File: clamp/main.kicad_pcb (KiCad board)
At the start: 2 copper layers, 36 parts, among them P1 CONN_01X12, U1 LM741, U2 LM741, U3 LM741, U4 LM741, U5 LM741, U6 LM741

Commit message: update
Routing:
- net -VE: track 307.7 -> 304.4 mm
- net OUT: track 192.5 -> 189.2 mm
- net +VE: track 291.6 -> 288.6 mm
- net I-SET: track 34.3 -> 33.3 mm
- net V-SET: track 48.0 -> 48.9 mm

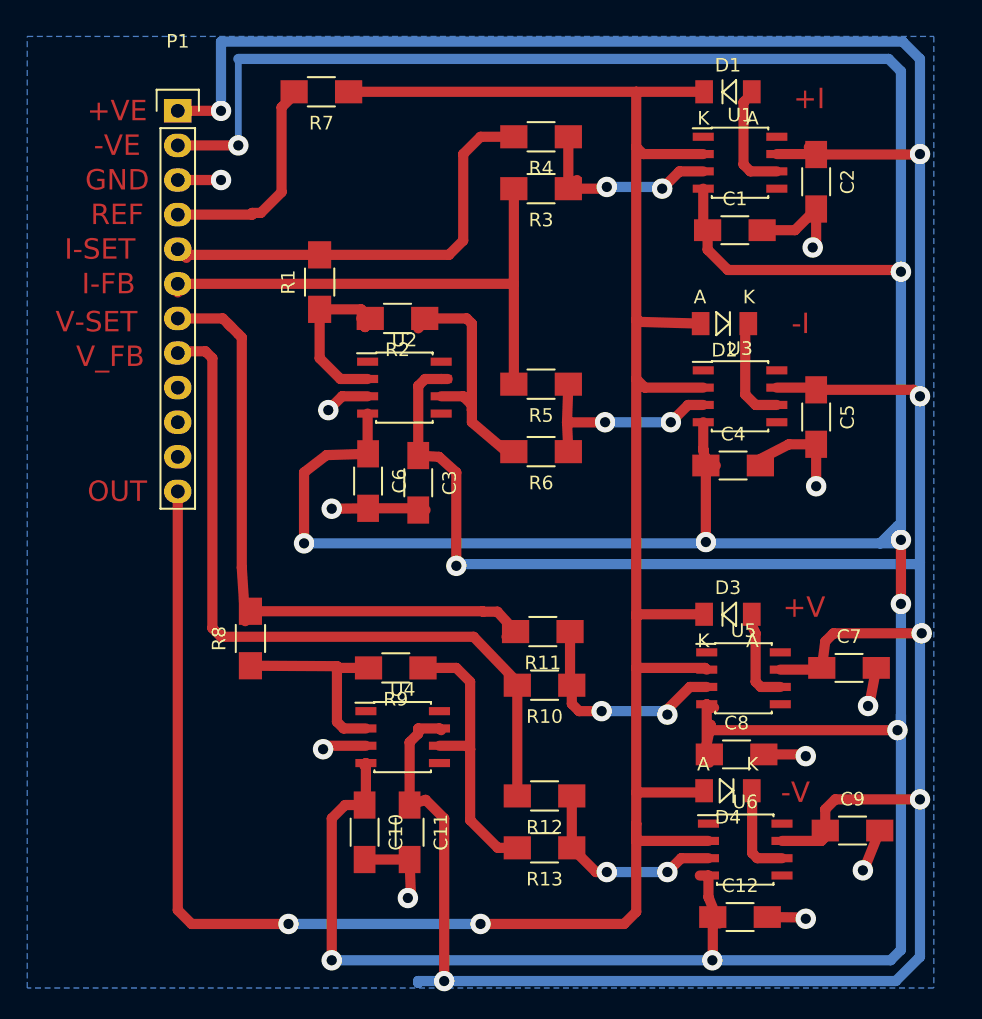
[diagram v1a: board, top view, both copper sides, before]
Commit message: add 0R values
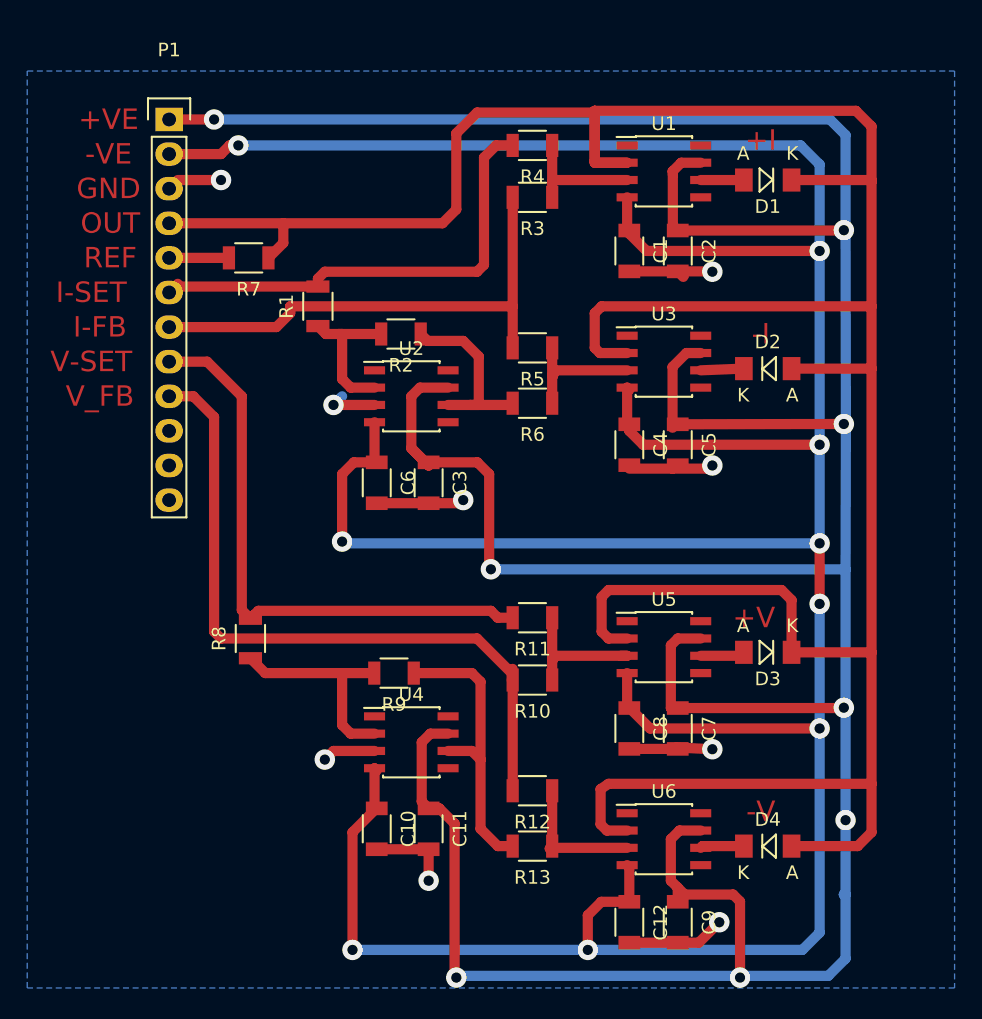
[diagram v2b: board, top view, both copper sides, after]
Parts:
- C1, C10, C11, C12, C2, C3, C4, C5, C6, C7, C8, C9: footprint Capacitors_SMD:C_1206_HandSoldering -> Capacitors_SMD:C_1206
- R1, R10, R11, R12, R13, R2, R3, R4, R5, R6, R7, R8, R9: footprint Resistors_SMD:R_1206_HandSoldering -> Resistors_SMD:R_1206
- moved C9 14.5 mm to (155.4, 145.3), turned to 270 degrees
- moved C7 13.3 mm to (155.4, 131.1), turned to 270 degrees
- moved R7 13.3 mm to (124.0, 96.5)
- moved C2 11.4 mm to (155.4, 96.0)
- moved C5 10.4 mm to (155.4, 110.2)
- moved C12 8.14 mm to (151.9, 145.3), turned to 270 degrees
- moved C8 8.10 mm to (151.9, 131.1), turned to 270 degrees
- moved C1 7.90 mm to (151.9, 96.0), turned to 270 degrees
- moved C4 7.77 mm to (151.9, 110.2), turned to 270 degrees
- moved D1 7.11 mm to (162.1, 90.8), turned to 180 degrees
- moved U5 6.27 mm to (154.4, 125.1)
- moved U3 6.14 mm to (154.4, 104.1)
- moved U6 6.02 mm to (154.4, 139.2)
- moved U1 5.62 mm to (154.4, 90.2)
- moved D4 5.00 mm to (162.1, 139.7), turned to 0 degrees
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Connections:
- P1 pad 12: OUT -> (no net)
- P1 pad 4: REF -> OUT
- P1 pad 5: I-SET -> REF
- P1 pad 6: I-FB -> I-SET
- P1 pad 7: V-SET -> I-FB
- P1 pad 8: V-FB -> V-SET
- P1 pad 9: (no net) -> V-FB
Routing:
- net -VE: track 304.4 -> 263.5 mm
- net OUT: track 189.2 -> 223.4 mm, vias 2 -> 0
- net REF: track 16.3 -> 4.72 mm
- net Net-(R10-Pad1): track 17.7 -> 10.8 mm, vias 2 -> 0
- net Net-(R3-Pad1): track 15.2 -> 9.36 mm, vias 2 -> 0
- net V-SET: track 48.9 -> 43.3 mm
- net V-FB: track 58.0 -> 52.3 mm
- net Net-(R5-Pad1): track 15.5 -> 9.90 mm, vias 2 -> 0
- net Net-(R12-Pad1): track 15.6 -> 10.1 mm, vias 2 -> 0
- net Net-(D1-Pad2): track 8.46 -> 3.17 mm
- net Net-(D2-Pad1): track 7.94 -> 3.17 mm
- net Net-(R2-Pad1): track 18.1 -> 13.9 mm
- net Net-(D4-Pad1): track 6.93 -> 3.22 mm
- net Net-(D3-Pad2): track 6.98 -> 3.28 mm
- net I-FB: track 40.4 -> 37.2 mm
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
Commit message: increased vias
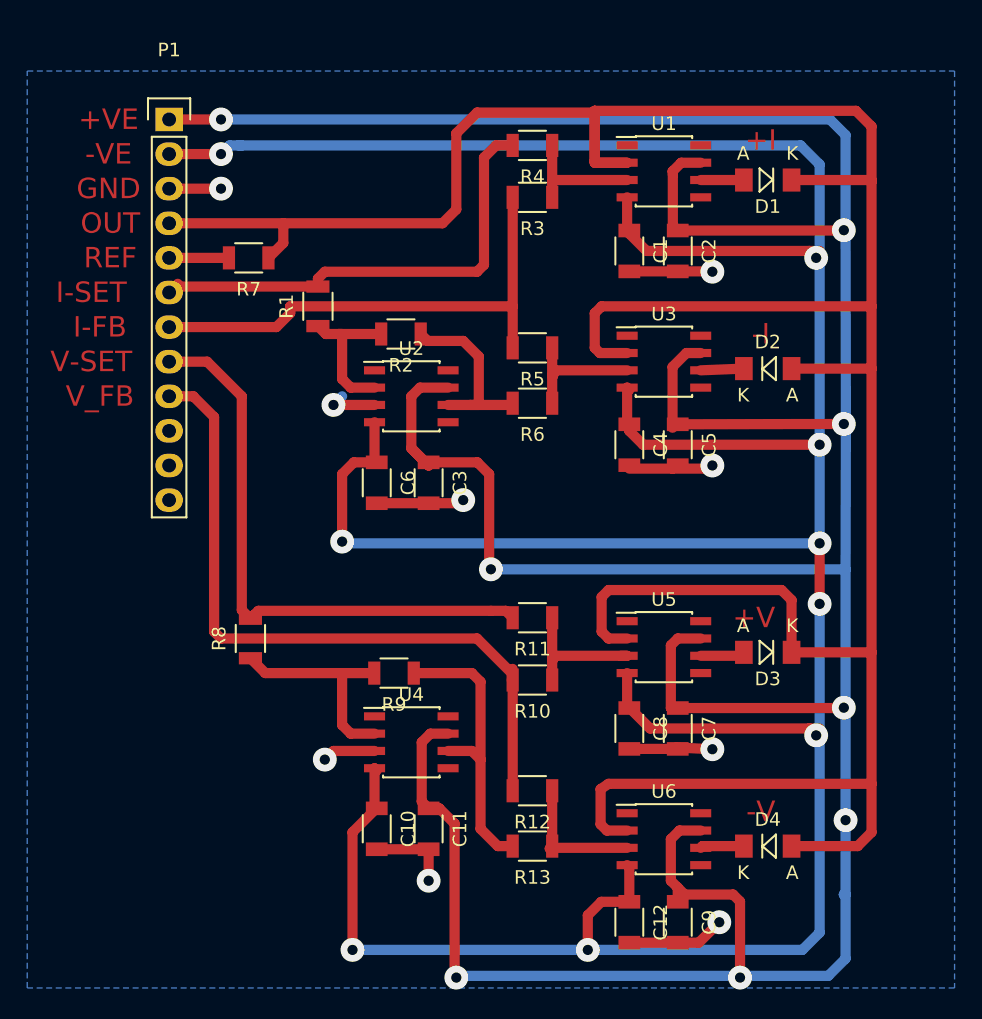
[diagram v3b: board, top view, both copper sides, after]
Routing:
- net -VE: track 263.5 -> 266.7 mm
- net GND: track 50.1 -> 49.4 mm
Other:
- net class Default: via_dia 1.5 -> 1.75

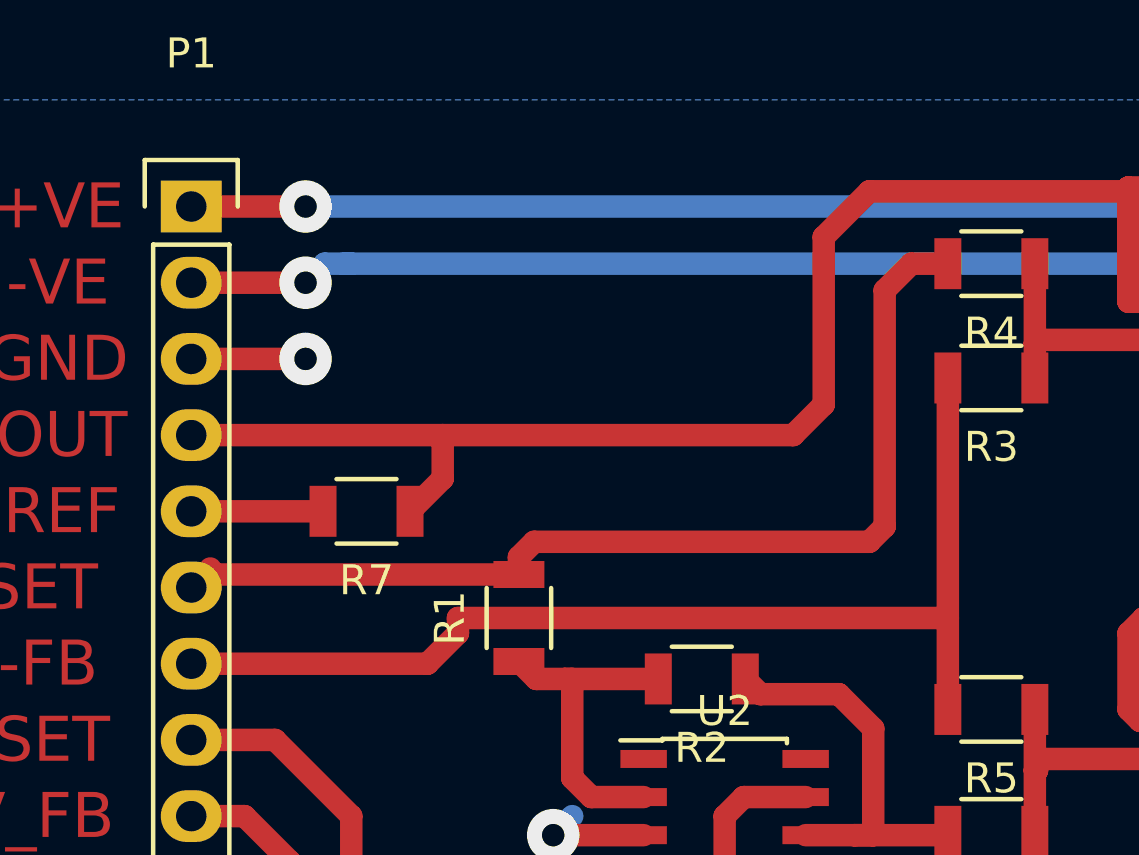
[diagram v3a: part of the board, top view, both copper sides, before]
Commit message: added heirarchical sheet
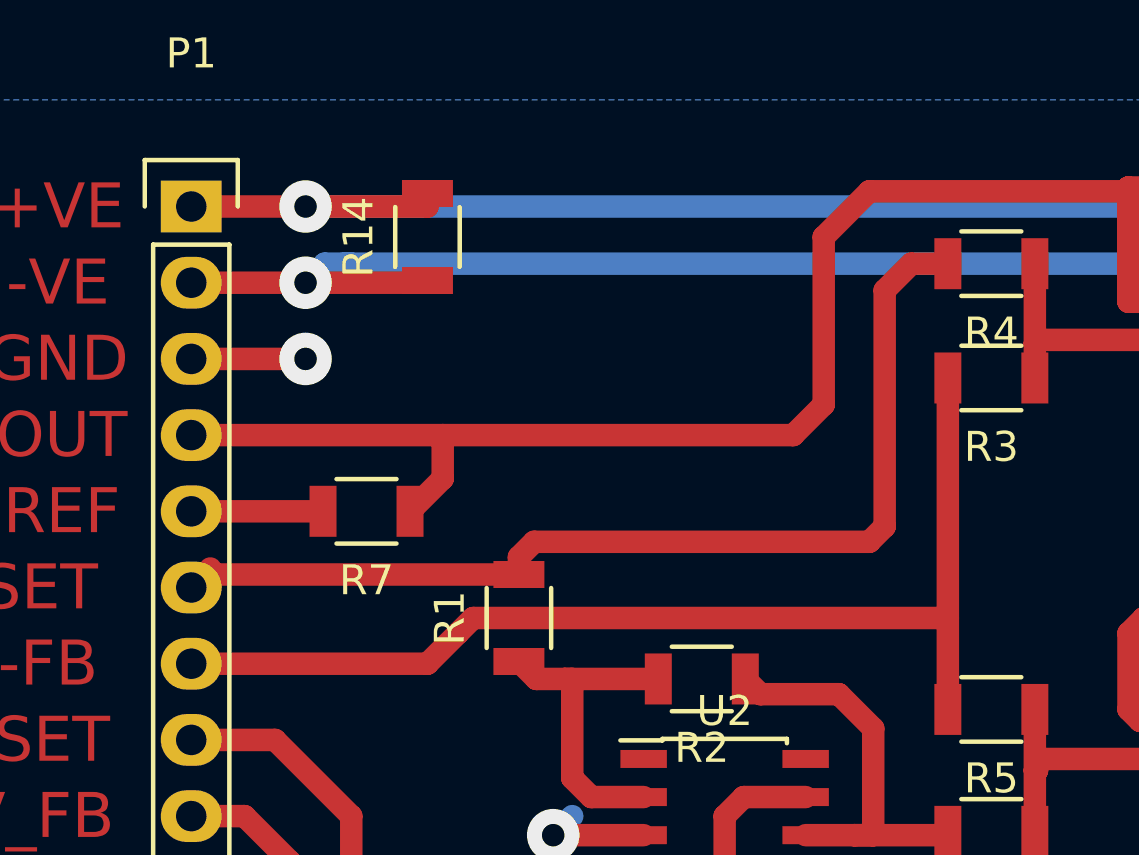
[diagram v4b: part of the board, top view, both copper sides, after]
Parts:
- added R14: R, Resistors_SMD:R_1206, F.Cu at (126.0, 87.4)
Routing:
- net +VE: track 287.6 -> 292.1 mm
- net -VE: track 266.7 -> 270.8 mm
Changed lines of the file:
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@@
 (kicad_pcb (version 4) (host pcbnew 4.0.4+dfsg1-stable)
   (general
-    (links 76)
+    (links 78)
     (no_connects 0)
-    (area 107.696 79.985 175.768001 151.352002)
+    (area 107.696 71.442999 175.768001 151.352002)
     (thickness 1.6)
     (drawings 13)
-    (tracks 339)
+    (tracks 343)
     (zones 0)
-    (modules 36)
+    (modules 37)
     (nets 22)
   )
@@
   (layers
     (0 F.Cu signal)
-    (31 B.Cu signal)
+    (31 B.Cu signal hide)
     (32 B.Adhes user)
     (33 F.Adhes user)
@@
     )
   )
+  (module Resistors_SMD:R_1206 (layer F.Cu)
+    (at 125.984 87.376 90)
+    (descr "Resistor SMD 1206, reflow soldering, Vishay (see dcrcw.pdf)")
+    (tags "resistor 1206")
+    (attr smd)
+    (fp_text reference R14 (at 0 -2.3 90) (layer F.SilkS)
+      (effects (font (size 1 1) (thickness 0.15)))
+    )
+    (fp_text value R (at 0 2.3 90) (layer F.Fab)
+      (effects (font (size 1 1) (thickness 0.15)))
+    )
+    (fp_line (start -2.2 -1.2) (end 2.2 -1.2) (layer F.CrtYd) (width 0.05))
+    (fp_line (start -2.2 1.2) (end 2.2 1.2) (layer F.CrtYd) (width 0.05))
+    (fp_line (start -2.2 -1.2) (end -2.2 1.2) (layer F.CrtYd) (width 0.05))
+    (fp_line (start 2.2 -1.2) (end 2.2 1.2) (layer F.CrtYd) (width 0.05))
+    (fp_line (start 1 1.075) (end -1 1.075) (layer F.SilkS) (width 0.15))
+    (fp_line (start -1 -1.075) (end 1 -1.075) (layer F.SilkS) (width 0.15))
+    (pad 1 smd rect (at -1.45 0 90) (size 0.9 1.7) (layers F.Cu F.Paste F.Mask)
+      (net 2 -VE))
+    (pad 2 smd rect (at 1.45 0 90) (size 0.9 1.7) (layers F.Cu F.Paste F.Mask)
+      (net 1 +VE))
+    (model Resistors_SMD.3dshapes/R_1206.wrl
+      (at (xyz 0 0 0))
+      (scale (xyz 1 1 1))
+      (rotate (xyz 0 0 0))
+    )
+  )
   (gr_text -V (at 161.544 137.16) (layer F.Cu)
     (effects (font (size 1.5 1.5) (thickness 0.3)))
@@
     (effects (font (size 1.5 1.5) (thickness 0.3)))
   )
+  (segment (start 121.92 86.36) (end 125.984 86.36) (width 0.75) (layer F.Cu) (net 1))
+  (segment (start 125.984 86.36) (end 125.984 85.926) (width 0.75) (layer F.Cu) (net 1))
   (segment (start 155.448 142.748) (end 155.448 143.788) (width 0.75) (layer F.Cu) (net 1))
   (segment (start 154.94 142.24) (end 155.448 142.748) (width 0.75) (layer F.Cu) (net 1))
@@
   (segment (start 135.89 106.68) (end 135.89 110.49) (width 0.75) (layer F.Cu) (net 1))
   (segment (start 136.525 106.045) (end 135.89 106.68) (width 0.75) (layer F.Cu) (net 1))
+  (segment (start 121.92 88.9) (end 125.91 88.9) (width 0.75) (layer F.Cu) (net 2))
+  (segment (start 125.91 88.9) (end 125.984 88.826) (width 0.75) (layer F.Cu) (net 2))
   (segment (start 165.1 131.064) (end 165.608 131.572) (width 0.75) (layer F.Cu) (net 2))
   (via (at 165.608 131.572) (size 1.75) (drill 0.75) (layers F.Cu B.Cu) (net 2))
@@
   (segment (start 118.544 98.626) (end 118.11 99.06) (width 0.75) (layer F.Cu) (net 8) (status 30))
   (segment (start 118.745 99.06) (end 118.745 98.425) (width 0.75) (layer F.Cu) (net 8) (status 30))
-  (segment (start 118.11 101.6) (end 125.984 101.6) (width 0.75) (layer F.Cu) (net 9) (status 10))
-  (segment (start 127 100.584) (end 127 100.076) (width 0.75) (layer F.Cu) (net 9))
+  (segment (start 127.508 100.076) (end 127 100.584) (width 0.75) (layer F.Cu) (net 9))
   (segment (start 125.984 101.6) (end 127 100.584) (width 0.75) (layer F.Cu) (net 9))
-  (segment (start 143.33 100.076) (end 127 100.076) (width 0.75) (layer F.Cu) (net 9))
+  (segment (start 125.984 101.6) (end 118.11 101.6) (width 0.75) (layer F.Cu) (net 9) (status 10))
+  (segment (start 143.33 100.076) (end 127.508 100.076) (width 0.75) (layer F.Cu) (net 9))
   (segment (start 143.33 92.075) (end 143.33 100.076) (width 0.75) (layer F.Cu) (net 9) (status 10))
   (segment (start 143.33 100.076) (end 143.33 103.124) (width 0.75) (layer F.Cu) (net 9) (status 20))

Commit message: tidy
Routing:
- net OUT: track 223.4 -> 216.8 mm
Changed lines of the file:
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@@
     (thickness 1.6)
     (drawings 13)
-    (tracks 343)
+    (tracks 341)
     (zones 0)
     (modules 37)
@@
   (segment (start 157.988 132.588) (end 157.861 132.588) (width 0.75) (layer B.Cu) (net 4))
   (via (at 157.988 132.588) (size 1.75) (drill 0.75) (layers F.Cu B.Cu) (net 4))
+  (segment (start 149.352 85.852) (end 149.352 88.9) (width 0.75) (layer F.Cu) (net 5))
+  (segment (start 149.987 89.535) (end 151.732 89.535) (width 0.75) (layer F.Cu) (net 5))
+  (segment (start 149.479 89.027) (end 149.987 89.535) (width 0.75) (layer F.Cu) (net 5))
+  (segment (start 168.402 85.852) (end 168.656 85.852) (width 0.75) (layer F.Cu) (net 5))
+  (segment (start 168.656 85.852) (end 169.672 86.868) (width 0.75) (layer F.Cu) (net 5))
+  (segment (start 168.402 85.852) (end 149.352 85.852) (width 0.75) (layer F.Cu) (net 5))
+  (segment (start 169.672 90.932) (end 169.672 86.868) (width 0.75) (layer F.Cu) (net 5))
+  (segment (start 149.352 85.852) (end 148.844 85.852) (width 0.75) (layer F.Cu) (net 5))
   (segment (start 169.672 135.128) (end 169.672 138.684) (width 0.75) (layer F.Cu) (net 5))
   (segment (start 168.656 139.7) (end 163.80206 139.7) (width 0.75) (layer F.Cu) (net 5) (status 20))
@@
   (segment (start 149.733 103.505) (end 149.352 103.124) (width 0.75) (layer F.Cu) (net 5))
   (segment (start 139.192 87.376) (end 140.716 85.852) (width 0.75) (layer F.Cu) (net 5))
-  (segment (start 140.716 85.852) (end 149.352 85.852) (width 0.75) (layer F.Cu) (net 5))
-  (segment (start 149.352 85.852) (end 149.352 85.725) (width 0.75) (layer F.Cu) (net 5))
+  (segment (start 126.492 93.98) (end 138.176 93.98) (width 0.75) (layer F.Cu) (net 5))
+  (segment (start 138.176 93.98) (end 139.192 92.964) (width 0.75) (layer F.Cu) (net 5))
   (segment (start 139.192 92.964) (end 139.192 87.376) (width 0.75) (layer F.Cu) (net 5))
-  (segment (start 138.176 93.98) (end 139.192 92.964) (width 0.75) (layer F.Cu) (net 5))
+  (segment (start 140.716 85.852) (end 148.844 85.852) (width 0.75) (layer F.Cu) (net 5))
+  (segment (start 148.844 85.852) (end 149.352 85.852) (width 0.75) (layer F.Cu) (net 5))
   (segment (start 118.11 93.98) (end 126.492 93.98) (width 0.75) (layer F.Cu) (net 5) (status 10))
-  (segment (start 126.492 93.98) (end 138.176 93.98) (width 0.75) (layer F.Cu) (net 5))
   (segment (start 125.402 96.52) (end 125.476 96.52) (width 0.75) (layer F.Cu) (net 5) (status 30))
-  (segment (start 151.732 89.535) (end 149.479 89.535) (width 0.75) (layer F.Cu) (net 5) (status 10))
-  (segment (start 149.479 89.535) (end 149.352 89.408) (width 0.75) (layer F.Cu) (net 5))
-  (segment (start 149.352 89.408) (end 149.352 85.725) (width 0.75) (layer F.Cu) (net 5))
-  (segment (start 149.352 89.408) (end 149.352 85.725) (width 0.75) (layer F.Cu) (net 5))
   (segment (start 150.368 124.46) (end 149.86 123.952) (width 0.75) (layer F.Cu) (net 5))
   (segment (start 163.068 120.904) (end 150.368 120.904) (width 0.75) (layer F.Cu) (net 5))
@@
   (segment (start 169.672 135.128) (end 150.368 135.128) (width 0.75) (layer F.Cu) (net 5))
   (segment (start 150.368 135.128) (end 149.781846 135.518769) (width 0.75) (layer F.Cu) (net 5))
-  (segment (start 149.352 89.535) (end 149.352 89.408) (width 0.75) (layer F.Cu) (net 5))
-  (segment (start 149.352 89.408) (end 149.352 89.535) (width 0.75) (layer F.Cu) (net 5))
   (segment (start 163.80206 104.648) (end 169.672 104.648) (width 0.75) (layer F.Cu) (net 5) (status 10))
   (segment (start 163.80206 125.476) (end 169.672 125.476) (width 0.75) (layer F.Cu) (net 5) (status 10))
   (segment (start 163.80206 90.805) (end 169.672 90.805) (width 0.75) (layer F.Cu) (net 5) (status 10))
   (segment (start 169.672 90.805) (end 169.672 90.932) (width 0.75) (layer F.Cu) (net 5))
-  (segment (start 149.352 85.725) (end 168.529 85.725) (width 0.75) (layer F.Cu) (net 5))
-  (segment (start 169.672 86.868) (end 169.672 90.932) (width 0.75) (layer F.Cu) (net 5))
-  (segment (start 168.529 85.725) (end 169.672 86.868) (width 0.75) (layer F.Cu) (net 5))
   (segment (start 169.672 125.476) (end 169.672 135.128) (width 0.75) (layer F.Cu) (net 5))
   (segment (start 169.672 90.932) (end 169.672 100.076) (width 0.75) (layer F.Cu) (net 5))
   (segment (start 169.672 100.076) (end 169.672 104.648) (width 0.75) (layer F.Cu) (net 5))
   (segment (start 169.672 104.648) (end 169.672 125.476) (width 0.75) (layer F.Cu) (net 5))
-  (segment (start 151.732 89.535) (end 149.352 89.535) (width 0.75) (layer F.Cu) (net 5) (status 10))
   (segment (start 157.132 104.775) (end 160.30194 104.648) (width 0.75) (layer F.Cu) (net 6) (status 30))
   (segment (start 122.502 96.52) (end 118.11 96.52) (width 0.75) (layer F.Cu) (net 7) (status 30))
